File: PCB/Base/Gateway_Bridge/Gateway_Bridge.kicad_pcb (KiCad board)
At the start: 2 copper layers, 98.9 x 70.1 mm, 58 parts, among them J1 J_DIAG, J2 J_I2C2, J3 STM32_Breakout, J5 J_CAN_TERM, J6 J_I2C1, J7 J_SWD, J8 J_BUS_IN, J9 J_BUS_OUT, SW1 RESET, U1 STM32F103C8Tx, U2 SN65HVD230, U3 AMS1117-3.3, U4 RP2040-ZERO, Y1 8MHz

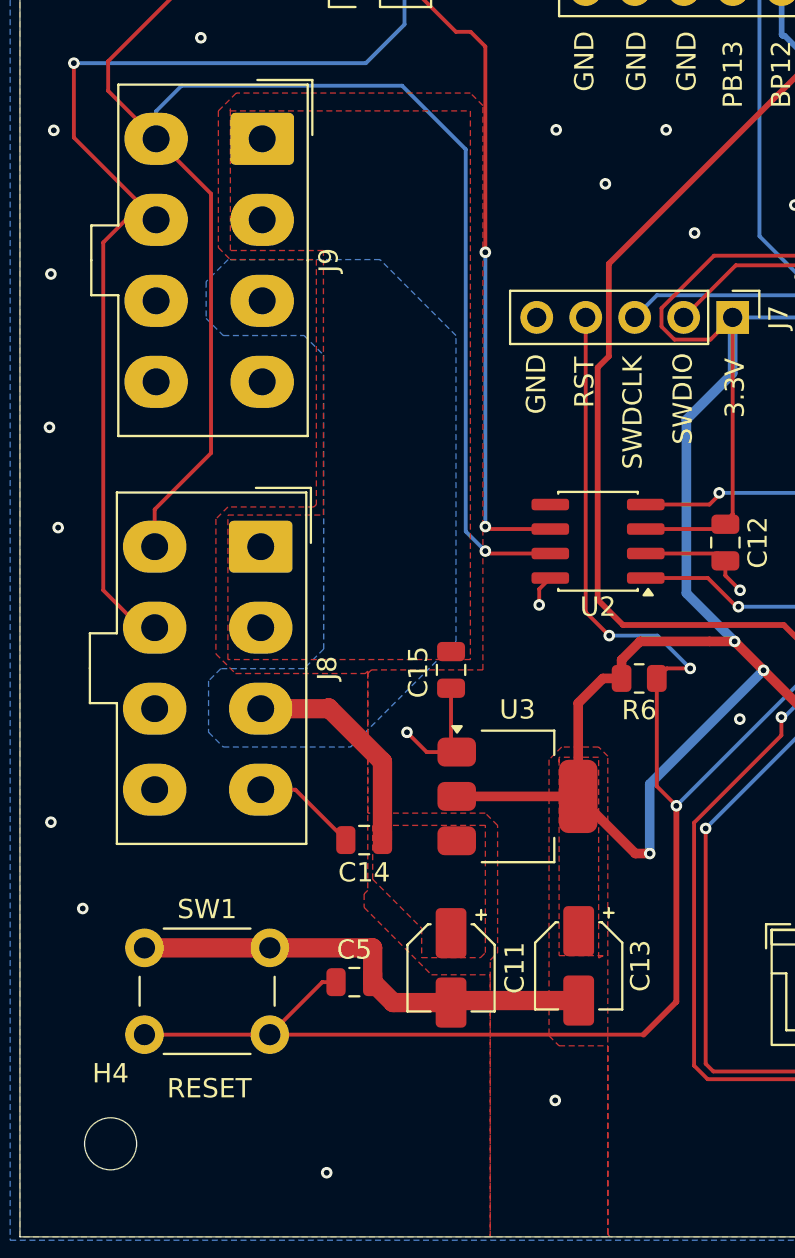
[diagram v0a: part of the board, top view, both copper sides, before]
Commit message: feat(pcb): input-rail TVS + AO3400A backlight FET + 35V bus cap on base boards
Roll the #214 input-rail TVS fleet standard into both base boards, plus
two margin upgrades folded into the same rev:

- Input-rail TVS at J_BUS_IN on both boards: SMBJ12A (+12V, C42368008)
  and SMBJ6.0A (+5V, C5331096), cathode->rail / anode->GND, 2-3 GND
  vias at each anode pad for a low-inductance clamp path. CAN-bus TVS
  intentionally excluded (SN65HVD230 has built-in +/-16kV HBM).
- Backlight FET IRLML2502 -> AO3400A (C49195711, PanelGroup only):
  30V Vds vs 20V for headroom over the 19.9V clamp; Vgs operational at
  2.5V so still 3.3V-driven.
- +12V bulk cap C15 25V -> 35V X5R (C49010152): DC-bias derating +
  clamp headroom. C14 (+5V) stays 25V.

LCSC/MP/Voltage carried in-symbol. Combined BOM CSV + InvenTree updated.
DRC/ERC clean on both boards.

Refs #214
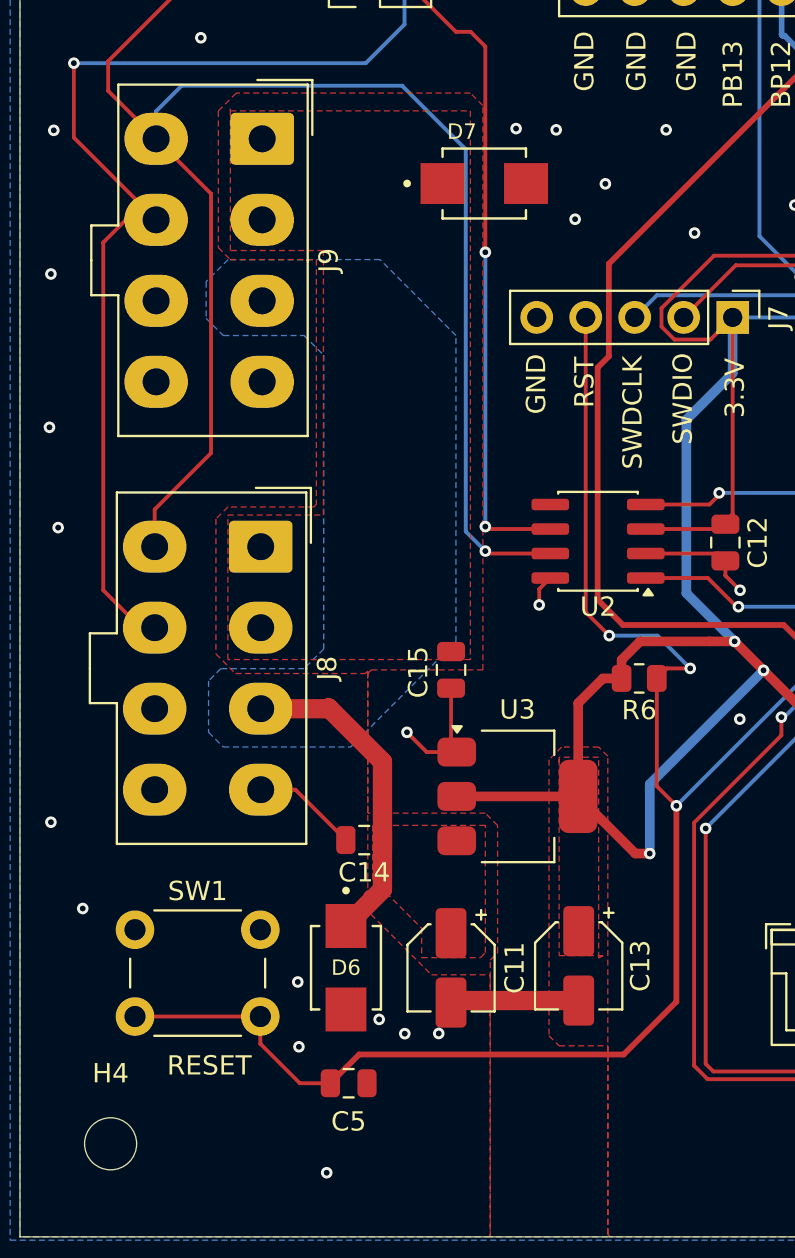
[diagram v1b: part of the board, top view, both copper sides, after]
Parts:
- added D6: SMBJ6.0A, OpenSkyhawk:DIOM4336X265N, F.Cu at (57.0, 137.6)
- added D7: SMBJ12A, OpenSkyhawk:DIOM4336X265N, F.Cu at (64.2, 97.0)
- moved C5 5.25 mm to (57.2, 143.6)
- moved SW1 1.06 mm to (46.1, 135.7)
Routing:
- net GND: track 127.1 -> 109.0 mm, vias 62 -> 68
- net +5V: track 11.6 -> 16.8 mm
- net /NRST: track 96.3 -> 95.5 mm

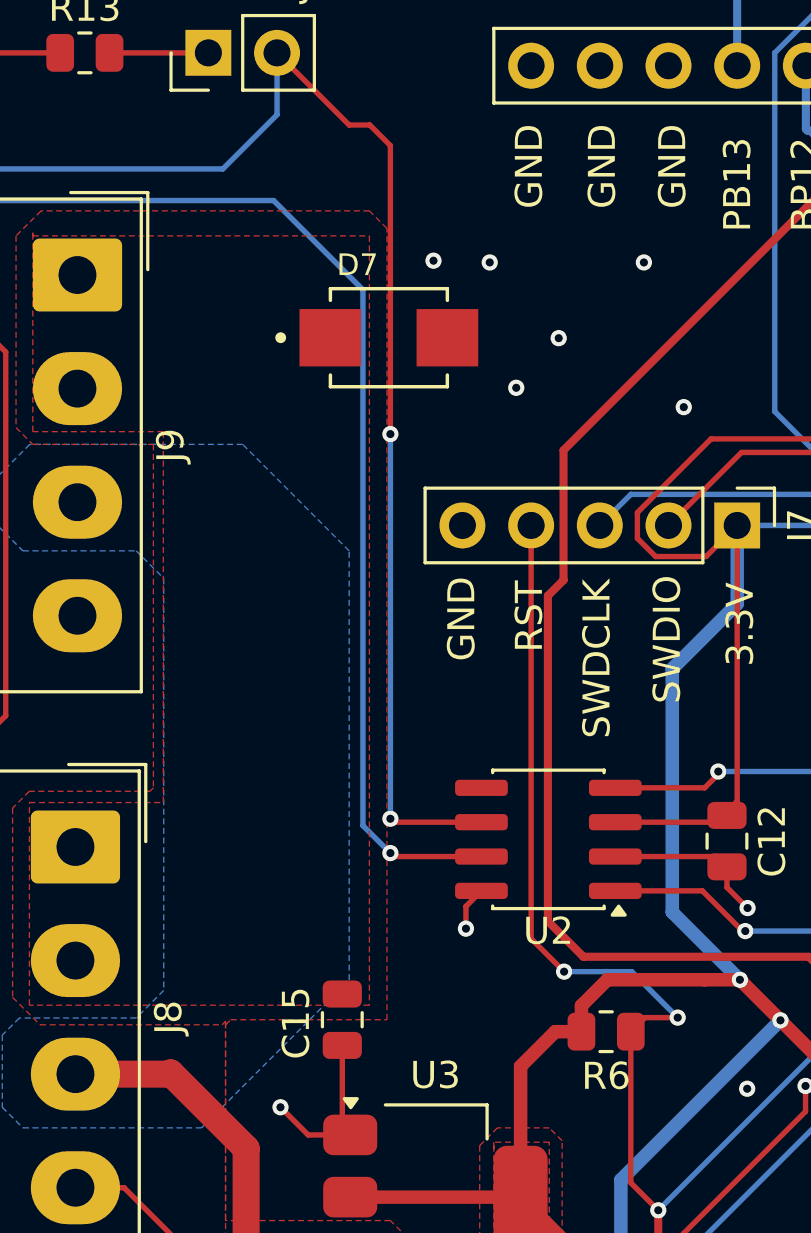
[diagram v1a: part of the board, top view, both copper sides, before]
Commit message: feat(pcb): +12V bulk cap → 22µF/35V electrolytic reroute (#236) (#243)
## What
Replaces the **+12V bulk cap** across ASN-41, PDU, Gateway_Bridge and
PanelGroup_Base:
**10µF/35V ceramic (0805) → 22µF/35V aluminium electrolytic**
`C48971029` (`Capacitor_SMD:CP_Elec_5x5.4`).

## Why (#236)
- 10µF/35V *ceramic* on a 12V rail DC-bias-derates to ~4–6µF;
electrolytic holds full value at ~1/5 the cost.
- Footprint grows 0805 → Ø5 (35V elec), so fabbed boards get a reroute;
value taken to 22µF (same Ø5 can) for margin.

## Changes
- Symbol fields updated: IPN `CAP-ELEC-22UF-35V-D5`, LCSC `C48971029`,
Rating `35V`, Tolerance `20%`.
- **PDU (C9), Gateway_Bridge (C15), PanelGroup_Base (C15)** — rerouted
for the Ø5 land; board revision **0.1.0 → 0.2.0**.
- **ASN-41 (C15)** — unrouted, schematic only; revision **0.1.0**.

## Verification
- ERC clean (0/0) on all four boards.
- CI (KiCad PR Reports) runs ERC/DRC.

Closes #236 — the +12V ceramic→electrolytic reroute was the
consolidation's last open action; the rest is decided and applied (per
#235 + this PR).
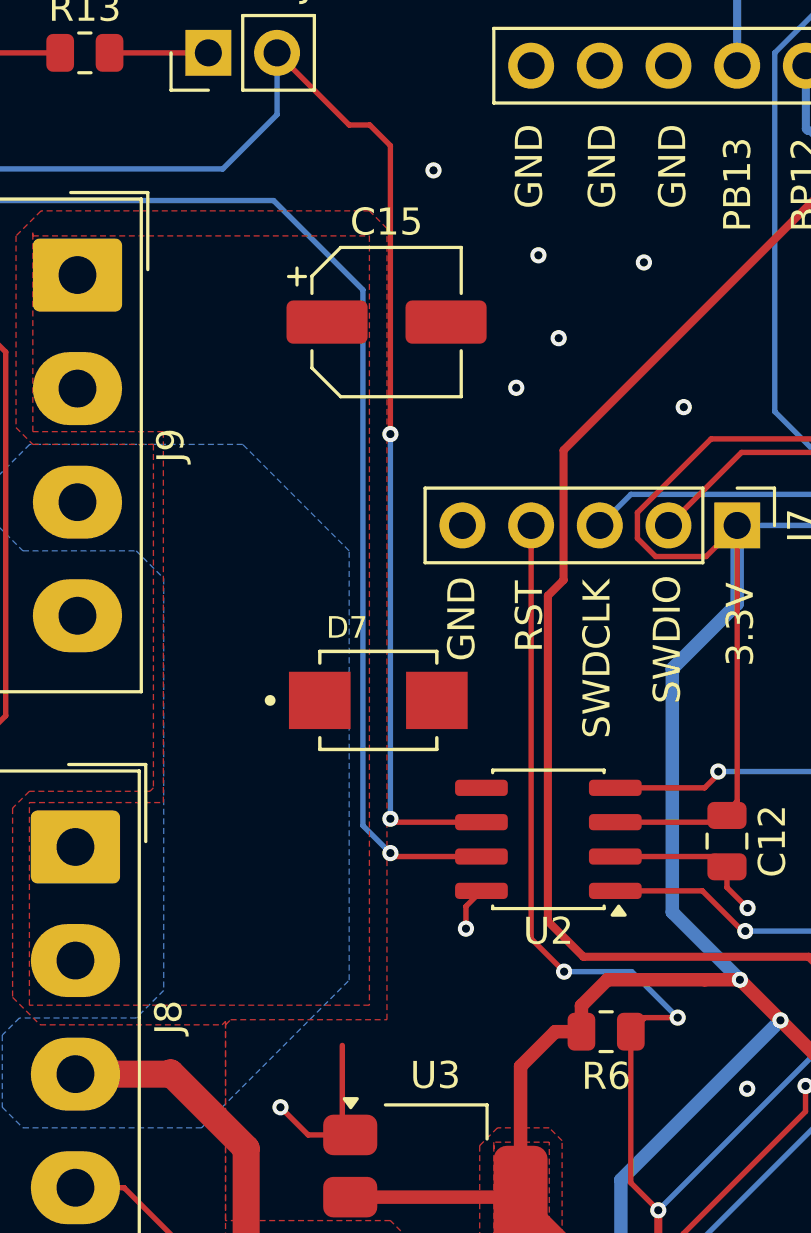
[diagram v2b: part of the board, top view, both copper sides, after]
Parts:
- C1: value 100nf -> 100nF
- C14: value 10uF -> 100nF
- C15: value 10uF -> 22uF; footprint Capacitor_SMD:C_0805_2012Metric -> Capacitor_SMD:CP_Elec_5x5.4
- R_BOOT1: value 10K -> 10k
- moved C15 25.8 mm to (64.1, 96.4), turned to 0 degrees
- moved D7 13.4 mm to (63.8, 110.4)

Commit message: fix(pcb): Gateway_Bridge silkscreen — connector pin labels and revision text (#209)
Prepares the board for the Rev 2 fab order. Silkscreen and field sync only;
no copper, footprint or netlist changes.

- J8/J9 (J_BUS_IN/J_BUS_OUT) had no pin labels at all. These carry 12V, 5V
  and CAN on unkeyed 8-pin Mini-Fit Jr connectors sitting side by side, so a
  reversed harness is destructive. Labelled 12V/12V/5V/GND/CANH/CANL/GND/GND.
- J1 (J_DIAG, the serial console) was labelled SDA/SCL — an I2C label set on a
  UART header. Corrected to RX/TX.
- J2/J6 (J_I2C2/J_I2C1) labelled SDA/SCL/3.3V/GND. Pins 1 and 2 carry
  auto-named nets because they pass through series resistors, traced through
  R11/R12 and R14/R15 to the host I2C nets.
- J5 CAN TERM legend moved to a free silk text. It had been made by overriding
  the footprint Value field, which raised a schematic-parity error and would
  have been wiped by the next sync.
- Revision text 0.1.0 -> "REVISION 0.2.0 | GATEWAY BRIDGE", stroke 0.15 to
  match the fleet.
- Update PCB from Schematic, picking up the IPN field on C15.

ERC 0, DRC 0 violations, 0 unconnected, 0 schematic parity.
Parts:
- moved G*** 0.64 mm to (82.9, 112.5)
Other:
- board text added: "12V"
- board text added: "5V"
- board text added: "CAN TERM"
- board text added: "CANH"
- board text added: "CANL"
- board text added: "REVISION 0.2.0 | GATEWAY BRIDGE"
- board text added: "RX"
- board text added: "SCL"
- board text added: "SDA"
- board text added: "TX"
- board text removed: "Revision 0.1.0"

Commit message: fix(pcb): Gateway UART series resistors R16/R17 33 Ω → 1k
The RP2040 runs only from USB and the STM32 from the bus, so either can be
unpowered while the other drives an idle-high TX into it. With 33 Ω the
unpowered chip is back-fed through its ESD diode at tens of mA; 1k caps it at
~3 mA, with ~10 ns edge cost against a 4 µs bit at 250 kbaud.

Fields only (Value, IPN RES-1K-1PCT-0805, LCSC C844939): same 0805 footprint,
no layout change, stencil unaffected. ERC 0, DRC 0, schematic parity 0.
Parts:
- R16, R17: value 33 -> 1k
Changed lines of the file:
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@@
 			)
 		)
-		(property "Value" "33"
+		(property "Value" "1k"
 			(at 0 1.65 0)
 			(layer "F.Fab")
@@
 			)
 		)
-		(property "IPN" "RES-33R-1PCT-0805"
+		(property "IPN" "RES-1K-1PCT-0805"
 			(at 0 0 0)
 			(unlocked yes)
@@
 			)
 		)
-		(property "LCSC" "C2090807"
+		(property "LCSC" "C844939"
 			(at 0 0 0)
 			(unlocked yes)
@@
 			)
 		)
-		(property "Value" "33"
+		(property "Value" "1k"
 			(at 0 1.65 0)
 			(layer "F.Fab")
@@
 			)
 		)
-		(property "IPN" "RES-33R-1PCT-0805"
+		(property "IPN" "RES-1K-1PCT-0805"
 			(at 0 0 0)
 			(unlocked yes)
@@
 			)
 		)
-		(property "LCSC" "C2090807"
+		(property "LCSC" "C844939"
 			(at 0 0 0)
 			(unlocked yes)

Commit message: fix(pcb): Gateway revision 0.2.0 → 0.2.1 for the R16/R17 change
Rev 0.2.0 was fabricated with 33 Ω at R16/R17; the 1k change makes the
schematic a new revision. Title block and silkscreen revision text only.
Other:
- board text added: "REVISION 0.2.1 | GATEWAY BRIDGE"
- board text removed: "REVISION 0.2.0 | GATEWAY BRIDGE"
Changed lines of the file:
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@@
 		)
 	)
-	(gr_text "REVISION 0.2.0 | GATEWAY BRIDGE"
+	(gr_text "REVISION 0.2.1 | GATEWAY BRIDGE"
 		(at 75.5 147.525 0)
 		(layer "B.SilkS")
